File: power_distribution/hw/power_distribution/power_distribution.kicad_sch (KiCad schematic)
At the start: 0 parts

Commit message: Set up sheets and add input stage
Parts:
- added C1: 47uF, symbol Device:C_Polarized_US
- added C2: 0.1uF, symbol Device:C
- added D1: D_TVS, symbol Device:D_TVS
- added F1: Fuse, symbol Device:Fuse
- added J1: Conn_01x02, Connector_AMASS:AMASS_XT30UPB-M_1x02_P5.0mm_Vertical, symbol Connector_Generic:Conn_01x02
- added Q1: Q_PMOS, symbol Device:Q_PMOS
- added R1: R, symbol Device:R
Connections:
- new net: D1.2 (A2), F1.2, Q1.S, R1.1
- new net GND: C1.2, C2.2, D1.1 (A1), J1.1 (Pin_1), Q1.G, R1.2
- new net VBAT_PROTECTED: C1.1, C2.1, Q1.D
- new net VBAT_RAW: F1.1, J1.2 (Pin_2)
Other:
- added sheet Stage 1: 43V2 to 12V (stage1.kicad_sch)
- added sheet Stage 2: 12V to 5V (stage2.kicad_sch)
- added sheet Stage 3: 5V to 3V3 (stage3.kicad_sch)
- company: (none) -> Author: Leopoldo Mendoza
- title: (none) -> Power Distribution Board - F25 Skateboard

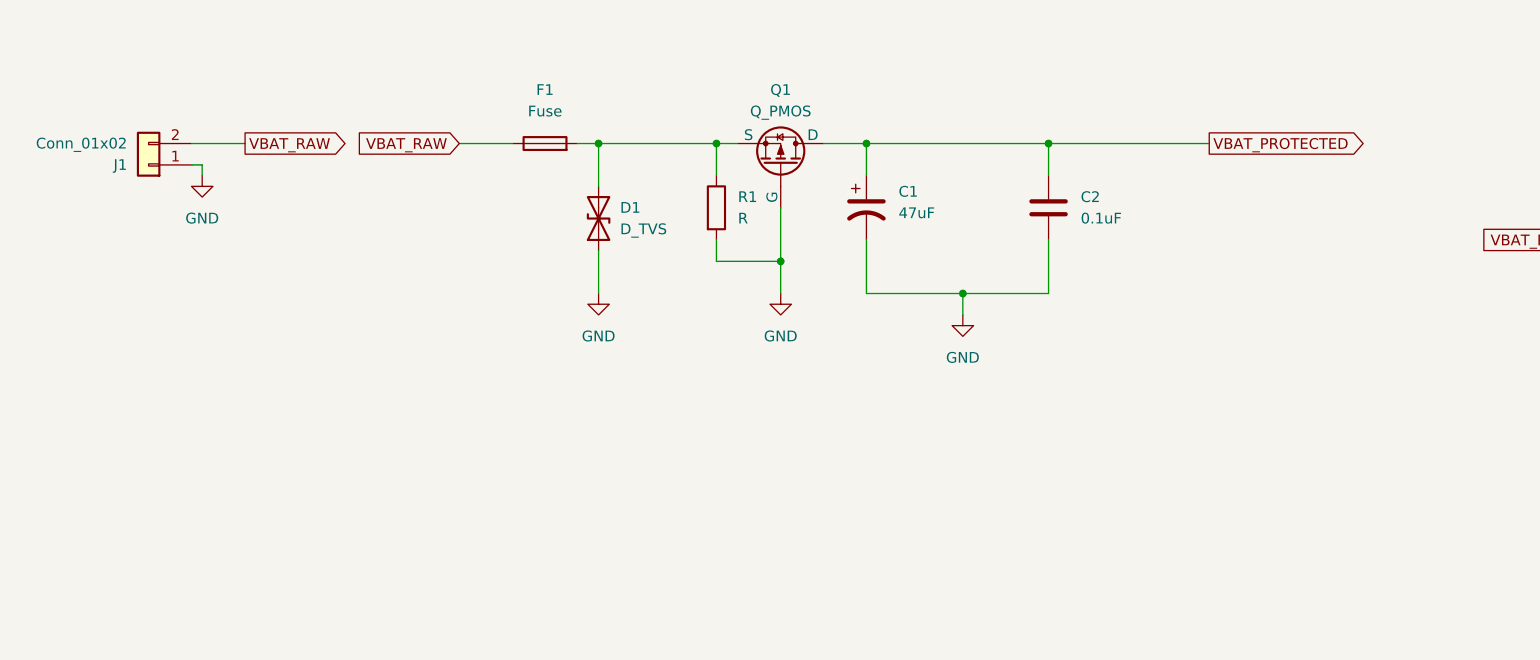
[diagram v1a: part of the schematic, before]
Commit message: Add telemetry libraries
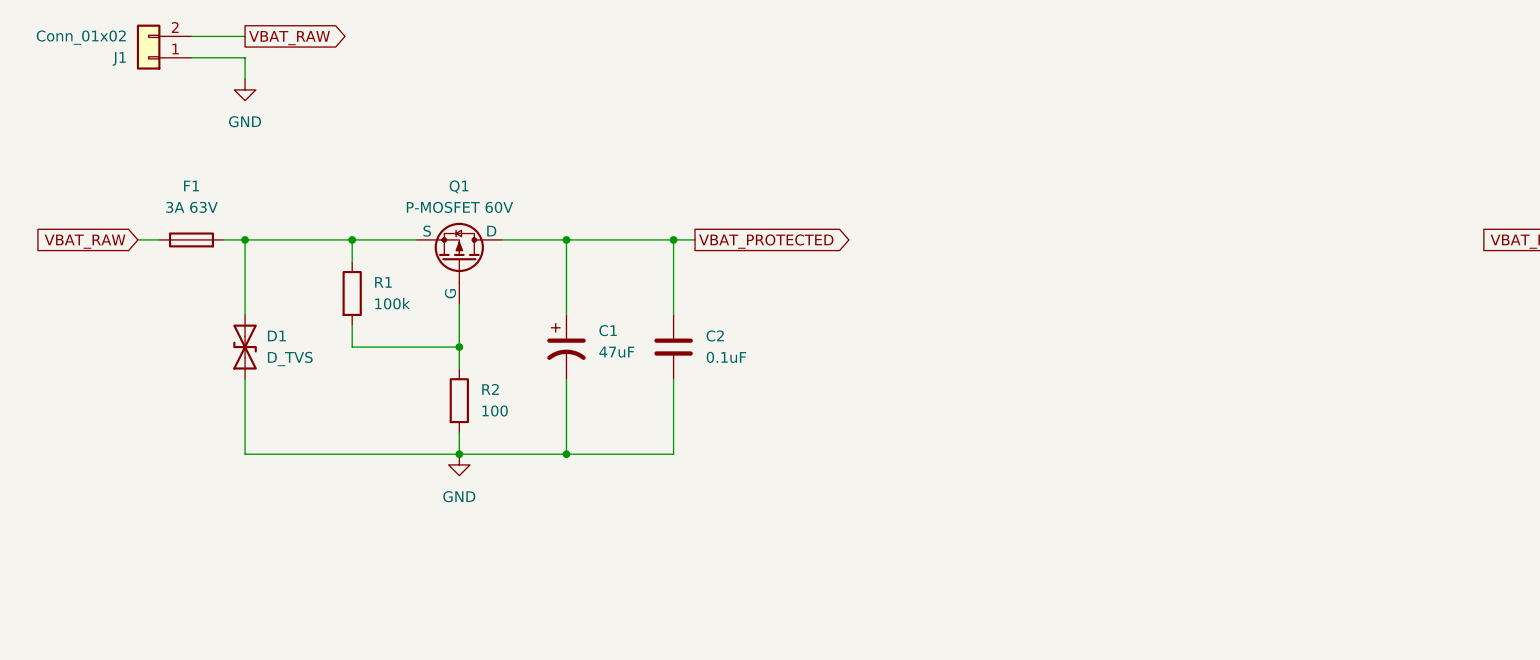
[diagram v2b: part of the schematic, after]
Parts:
- added R2: 100, symbol Device:R
- F1: value Fuse -> 3A 63V
- Q1: value Q_PMOS -> P-MOSFET 60V
- R1: value R -> 100k
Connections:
- net GND: now also R2.2; no longer Q1.G, R1.2
- new net: Q1.G, R1.2, R2.1
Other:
- moved on the sheet: C1, C2, D1, F1, J1, Q1, R1

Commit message: Finish Input stage
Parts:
- removed D1: D_TVS, symbol Device:D_TVS
- removed F1: 3A 63V, symbol Device:Fuse
- removed R2: 100, symbol Device:R
- added D1: TVS, SMBJ51A-13-F:DIOM5336X250N, symbol SMBJ51A-13-F:SMBJ51A-13-F
- added D2: 15V, BZT52C15-7-F:SOD3715X135N, symbol Device:D_Zener
- added U1: 3.5A 63V, C1_BEL, symbol 0685T3500-01:C1T_3.5
- Q1: value P-MOSFET 60V -> PMOS; footprint (none) -> GSFD6959:PMOSGDS_TO-252_DPAK_GAS
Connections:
- net GND: now also R1.2, D1.2
- net VBAT_PROTECTED: now also Q1.S, D2.1 (K); no longer Q1.D
- net VBAT_RAW: now also U1.1
- net at R1.1: now also Q1.G, D2.2 (A); no longer Q1.S
- new net: D1.1, Q1.D, U1.2
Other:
- sheet Stage 1: 43V2 to 12V renamed Stage 1: 43.2V to 12V
- moved on the sheet: C1, C2, J1, R1

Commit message: Finish output stage
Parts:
- removed U1: 3.5A 63V, C1_BEL, symbol 0685T3500-01:C1T_3.5
- added C3, C5, C7: 47uF, symbol Device:C_Polarized_US
- added C4, C6, C8: 0.1uF, symbol Device:C
- added D3, D6, D8: 2Vf, symbol Device:LED
- added D4: 12Vrwm, ESD5Z12T1G:SOD-523_0P9X1P3_ONS, symbol SMBJ51A-13-F:SMBJ51A-13-F
- added D5: 5Vrwm, ESD5Z5.0T1G:SOD-523_0P9X1P3_ONS, symbol SMBJ51A-13-F:SMBJ51A-13-F
- added D7: 3.3Vrwm, ESD5Z5.0T1G:SOD-523_0P9X1P3_ONS, symbol SMBJ51A-13-F:SMBJ51A-13-F
- added F1: 3.5A 63V, 0685T3500-01:C1_BEL, symbol Device:Fuse
- added F2, F3, F4: 0.5A 16V, 0ZCH0050FF2G:0ZCH_BEL, symbol Device:Polyfuse
- added J2, J3, J4: Conn_01x02, Connector_JST:JST_PH_S2B-PH-K_1x02_P2.00mm_Horizontal, symbol Connector_Generic:Conn_01x02
- added R2: 4.7k, symbol Device:R
- added R3: 1.5k, symbol Device:R
- added R4: 680, symbol Device:R
- D1: value TVS -> 51Vrwm
- D2: value 15V -> 15Vz
- Q1: value PMOS -> 60Vds
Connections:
- net 12V_BUS: now also F2.2
- net 5V_BUS: now also F3.2, F4.2
- net GND: now also C3.2, C4.2, C5.2, C6.2, C7.2, C8.2, D4.2, D5.2, D7.2, J2.1 (Pin_1), J3.1 (Pin_1), J4.1 (Pin_1), R2.1, R3.1, R4.1
- net at D1.1, Q1.D: now also F1.2
- net VBAT_PROTECTED renamed VBAT
- net VBAT_RAW: no longer names the net of J1.2 (Pin_2)
- net VBAT_RAW: now also F1.1
- new net: C3.1, C4.1, D3.1 (K), D4.1, F2.1, J2.2 (Pin_2)
- new net: C7.1, C8.1, D7.1, D8.1 (K), F4.1, J4.2 (Pin_2)
- new net: C5.1, C6.1, D5.1, D6.1 (K), F3.1, J3.2 (Pin_2)
- new net: D3.2 (A), R2.2
- new net: D6.2 (A), R3.2
- new net: D8.2 (A), R4.2
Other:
- note added: "Input"
- note added: "Output"
- moved on the sheet: C1, C2, D1, D2, J1, Q1, R1

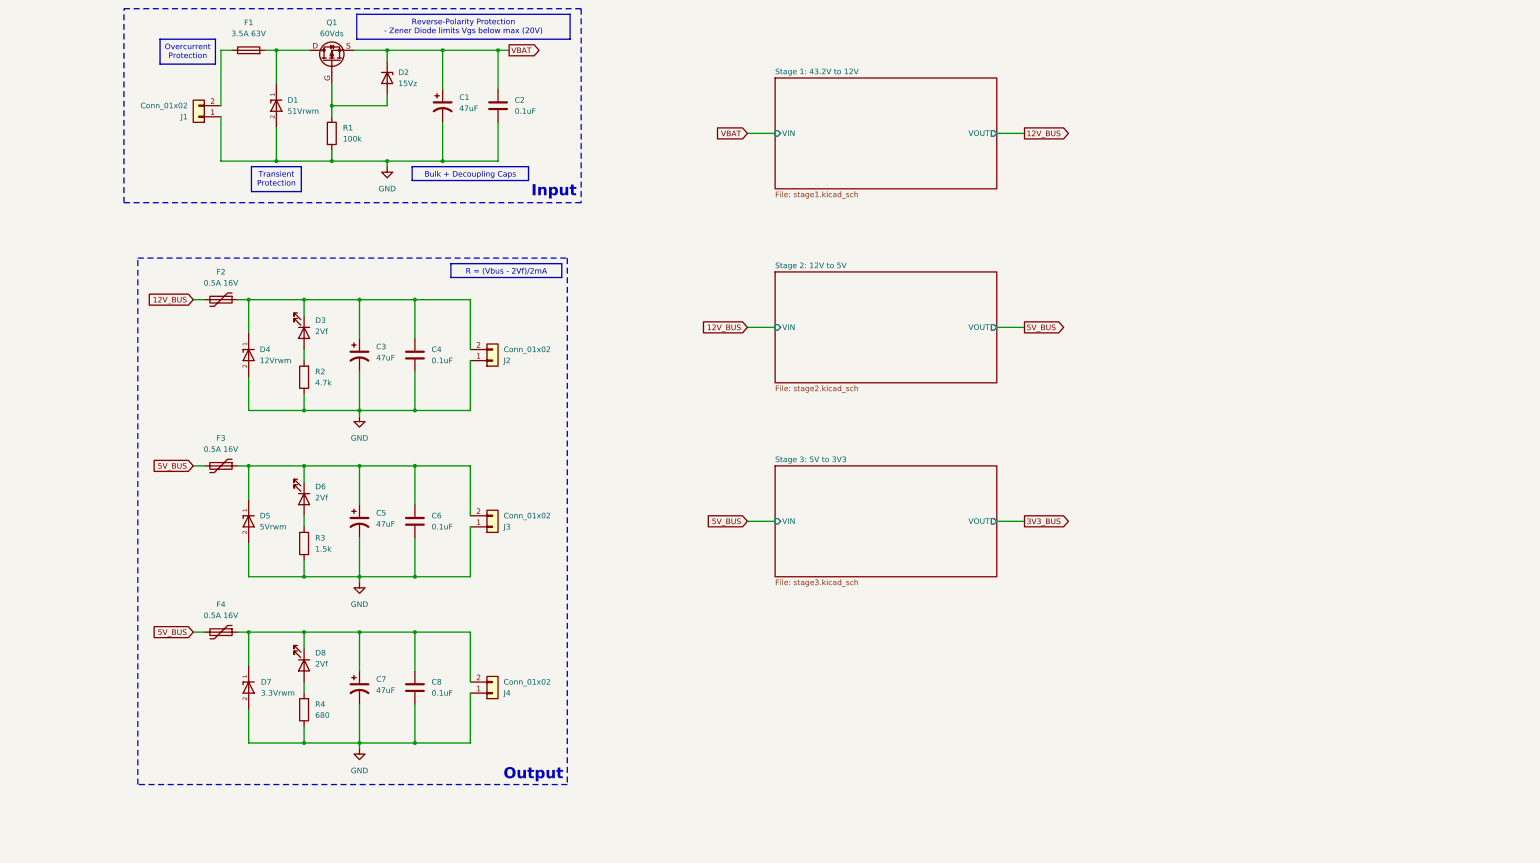
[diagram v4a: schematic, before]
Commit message: Finish stage 1 annotation and stage 2 and 3
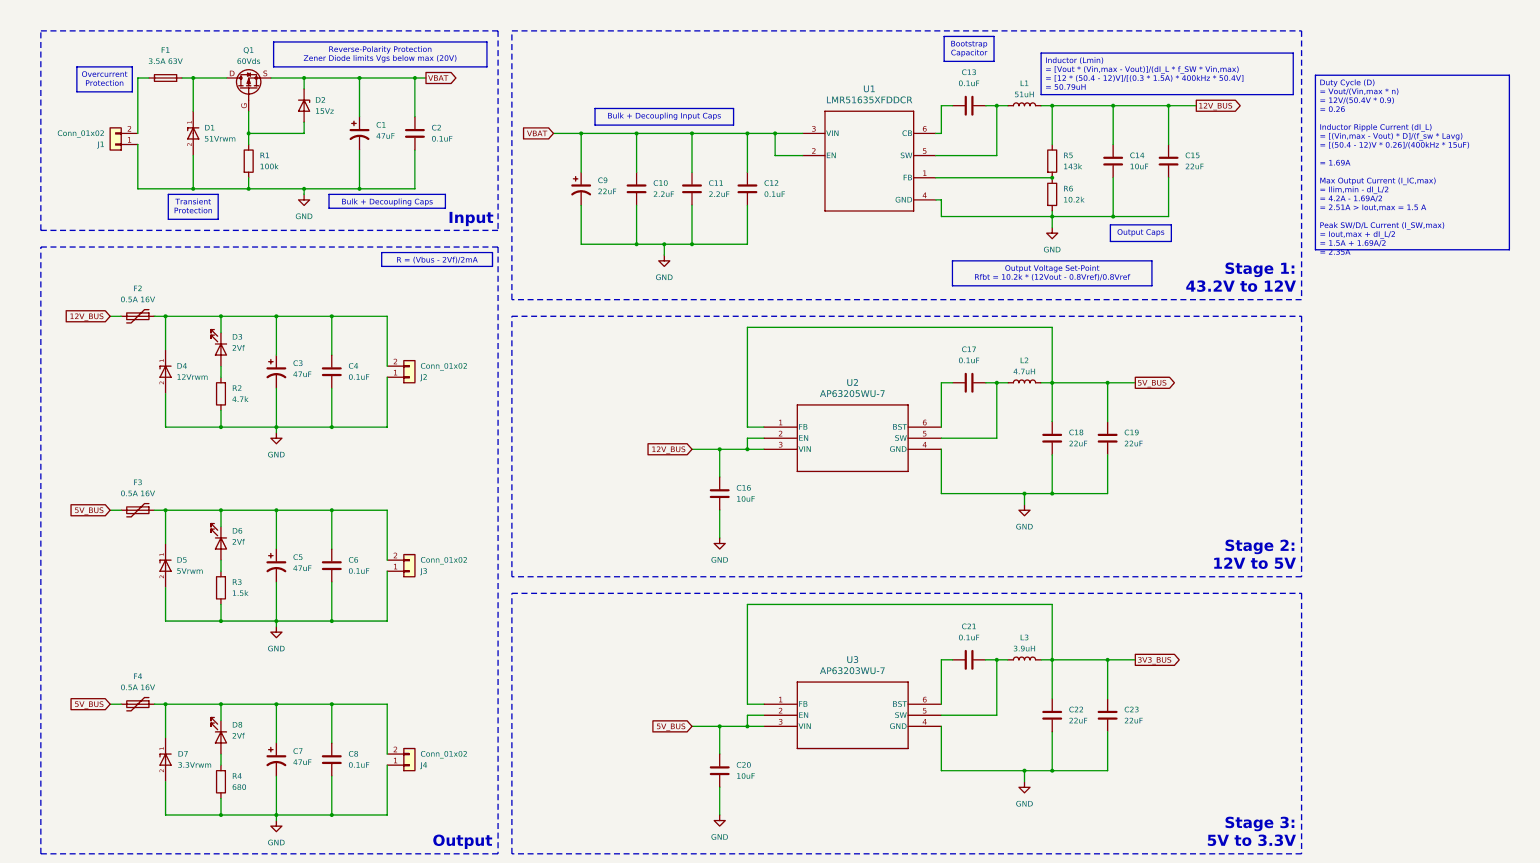
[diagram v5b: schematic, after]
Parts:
- added C10, C11: 2.2uF, symbol Device:C
- added C12, C13, C17, C21: 0.1uF, symbol Device:C
- added C14, C16, C20: 10uF, symbol Device:C
- added C15, C18, C19, C22, C23: 22uF, symbol Device:C
- added C9: 22uF, symbol Device:C_Polarized_US
- added L1: 51uH, symbol Device:L
- added L2: 4.7uH, symbol Device:L
- added L3: 3.9uH, symbol Device:L
- added R5: 143k, symbol Device:R
- added R6: 10.2k, symbol Device:R
- added U1: LMR51635XFDDCR, DDC0006A-MFG, symbol LMR51635XFDDCR:LMR51635XFDDCR
- added U2: AP63205WU-7, SOIC_05WU-7_DIO, symbol AP63205WU-7:AP63205WU-7
- added U3: AP63203WU-7, AP63203WU-7_DIO, symbol AP63203WU-7:AP63203WU-7
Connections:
- net 12V_BUS: now also C14.1, C15.1, C16.1, L1.2, R5.1, U2.2 (EN), U2.3 (VIN)
- net 3V3_BUS: now also C22.1, C23.1, L3.2, U3.1 (FB)
- net 5V_BUS: now also C18.1, C19.1, C20.1, L2.2, U2.1 (FB), U3.2 (EN), U3.3 (VIN)
- net GND: now also C10.2, C11.2, C12.2, C14.2, C15.2, C16.2, C18.2, C19.2, C20.2, C22.2, C23.2, C9.2, R6.2, U1.4 (GND), U2.4 (GND), U3.4 (GND)
- net VBAT: now also C10.1, C11.1, C12.1, C9.1, U1.2 (EN), U1.3 (VIN)
- new net: C17.2, L2.1, U2.5 (SW)
- new net: C17.1, U2.6 (BST)
- new net: R5.2, R6.1, U1.1 (FB)
- new net: C13.2, L1.1, U1.5 (SW)
- new net: C13.1, U1.6 (CB)
- new net: C21.1, U3.6 (BST)
- new net: C21.2, L3.1, U3.5 (SW)
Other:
- removed sheet Stage 1: 43.2V to 12V
- removed sheet Stage 2: 12V to 5V
- removed sheet Stage 3: 5V to 3V3
- note added: "Stage 1: 43.2V to 12V"
- note added: "Stage 2: 12V to 5V"
- note added: "Stage 3: 5V to 3.3V"
- moved on the sheet: C1, C2, C3, C4, C5, C6, C7, C8, D1, D2, D3, D4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

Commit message: Finished rev 1
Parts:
- D1: footprint SMBJ51A-13-F:DIOM5336X250N -> SMBJ51A-13-F:SMB_DIO
- J1: value Conn_01x02 -> XT30-M_Ver
- J2, J3, J4: value Conn_01x02 -> JST-PH_01x02
- U1: footprint DDC0006A-MFG -> LMR51635XFDDCR:DDC0006A-MFG
- U2: footprint SOIC_05WU-7_DIO -> AP63205WU-7:SOIC_05WU-7_DIO
- U3: footprint AP63203WU-7_DIO -> AP63203WU-7:AP63203WU-7_DIO
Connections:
- net 3V3_BUS: now also F4.2
- net 5V_BUS: no longer F4.2
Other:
- moved on the sheet: C1, C2, D1, D2, F1, J1, Q1, R1
